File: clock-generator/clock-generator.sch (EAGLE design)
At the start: 39 parts, among them U1 SN74LVC1G04DBV, U3 ATSAMD11-QFN24, U4 SI5351C, X1 MINI-USB-SHIELD-UX60A-MB-5ST, X2 JACK2.5_SJ-2523

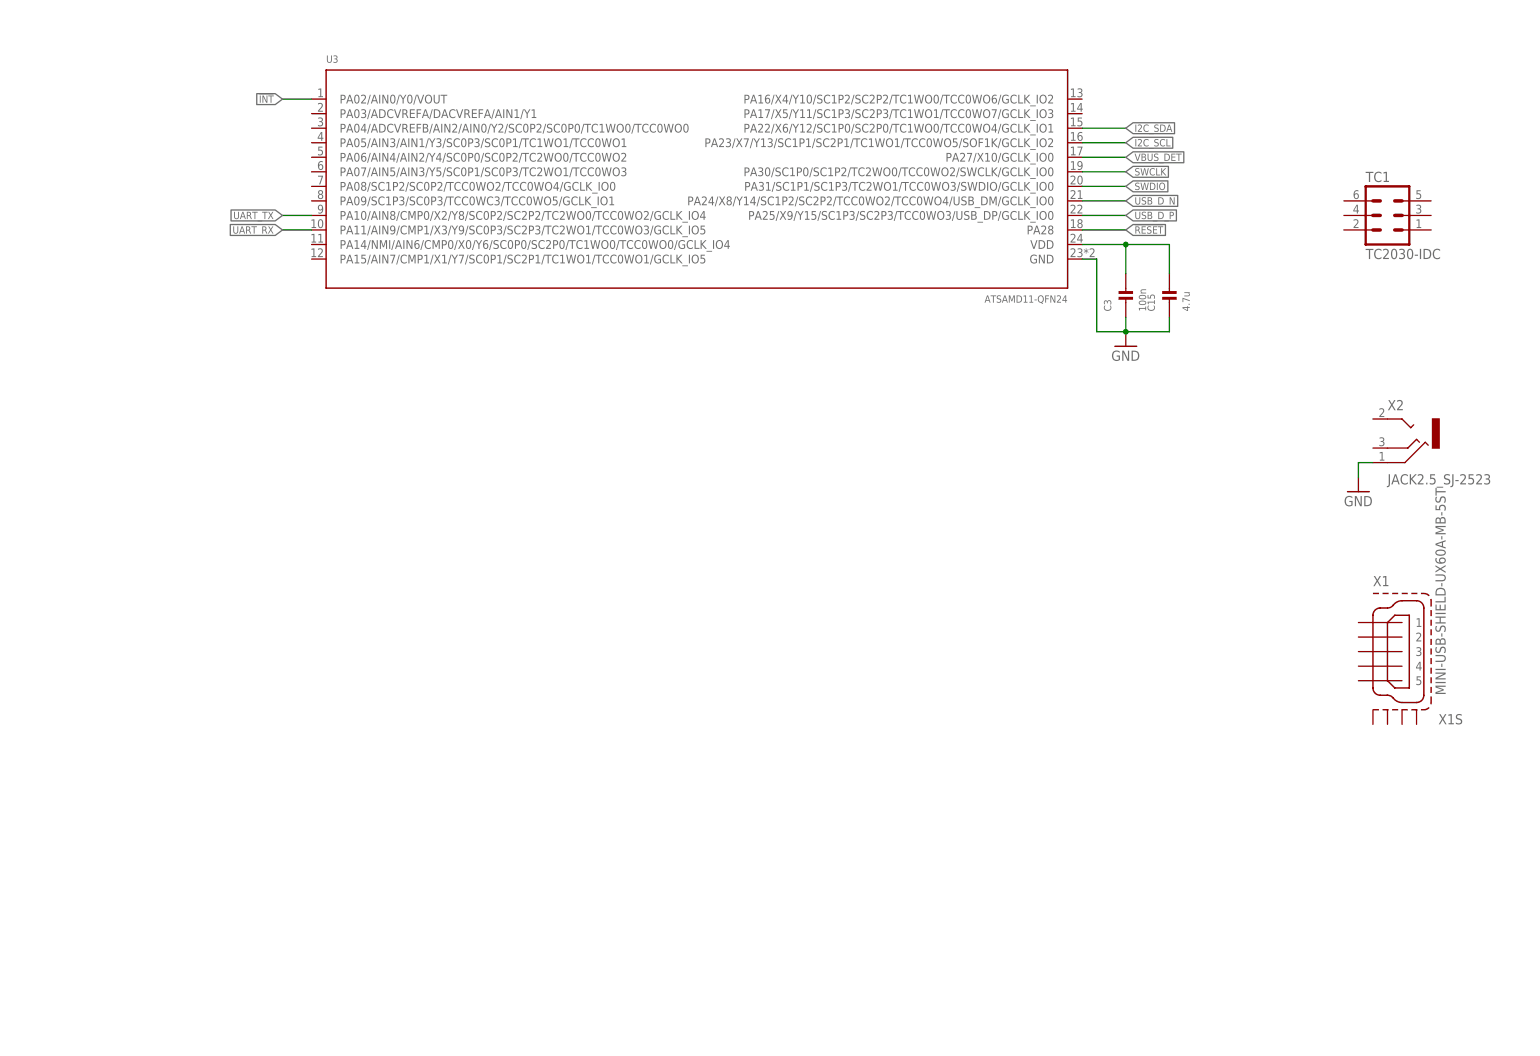
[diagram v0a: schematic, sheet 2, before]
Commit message: clock-generator: More work on schematics (USB, UART, ESD)
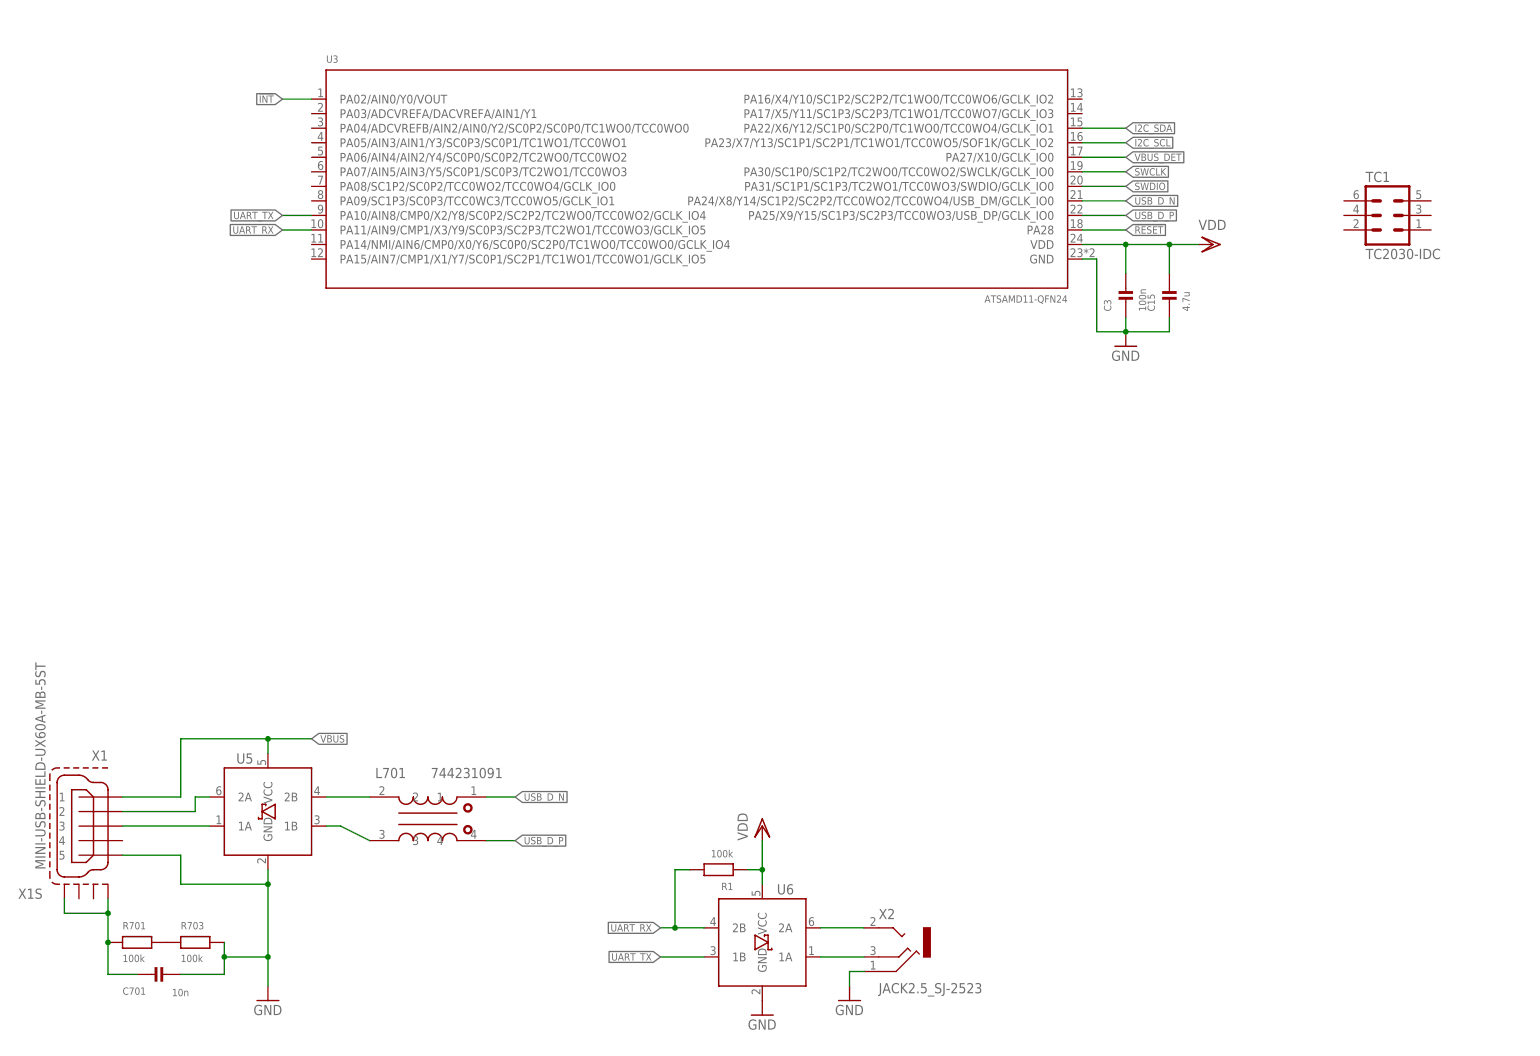
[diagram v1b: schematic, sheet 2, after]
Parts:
- added C701: 10n, rc-sysmocom:CAP_CERAMIC_0402
- added D1, D2, D3, D4, D5, D6, D7, D8, D9: 0603ESDA-TR, laforge:0603ESDA-TR
- added L701: 744231091, Wuerth_Elektronik_eiSos_V6_20140807:WE-CNSW_0805
- added R1, R701, R703: 100k, rc-sysmocom:RESISTOR_0603
- added R2, R3: 2k2, rc-sysmocom:RESISTOR_0603
- added U5, U6: IP4234CZ6, laforge:IP4234CZ6
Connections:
- removed net N$2: C15.2, C3.2, U3.VDD
- removed net N$4: JP1.1, R8.2, U1G1.I
- new net N$22: L701.2, U5.2B
- new net N$43: L701.3, U5.1B
- new net N$55: R701.1, R703.2
- new net N$6: U6.2A, X2.TIP
- new net N$61: C701.1, R701.2, X1S.S1, X1S.S4
- new net N$8: U6.1A, X2.MIDDLE
- new net USB0_D_N: U5.2A, X1G$1.2
- new net USB0_D_P: U5.1A, X1G$1.3
- new net VBUS: U5.VCC, X1G$1.1
- net CLK0_LINE: now also D1.K
- net CLK1_LINE: now also D2.K
- net CLK2_LINE: now also D3.K
- net CLK3_LINE: now also D4.K
- net CLK4_LINE: now also D5.K
- net CLK5_LINE: now also D6.K
- net CLK6_LINE: now also D7.K
- net CLK7_LINE: now also D8.K
- net CLKIN_AC: now also D9.K, JP1.1, R8.2, U1G1.I
- net GND: now also C701.2, D1.A, D2.A, D3.A, D4.A, D5.A, D6.A, D7.A, D8.A, D9.A, R703.1, U5.GND, U6.GND, X1G$1.5
- net I2C_SCL: now also R3.2
- net I2C_SDA: now also R2.2
- net UART_RX: now also R1.1, U6.2B
- net UART_TX: now also U6.1B
- net USB_D_N: now also L701.1
- net USB_D_P: now also L701.4
- net VDD: now also C15.2, C3.2, R1.2, R2.1, R3.1, U3.VDD, U6.VCC
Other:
- moved on the sheet: Q3, X1, X1S, X2

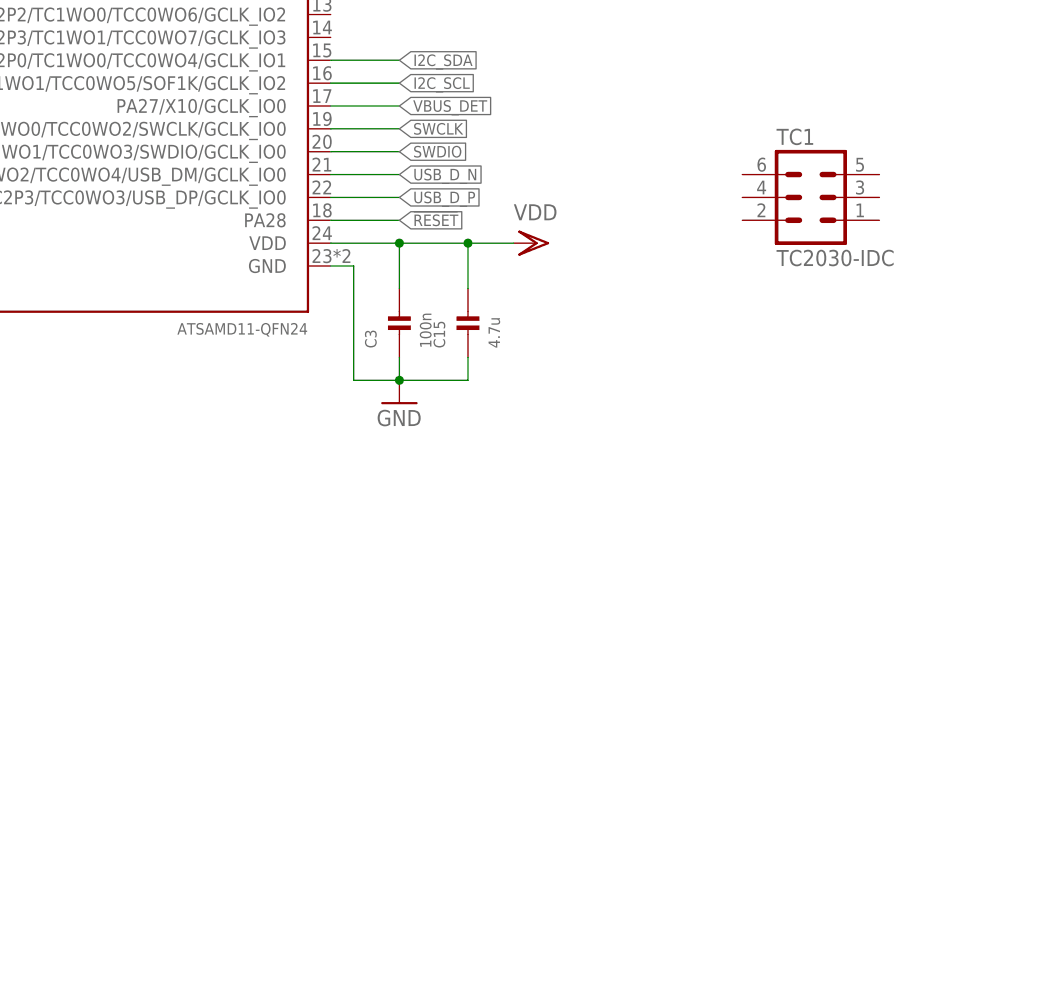
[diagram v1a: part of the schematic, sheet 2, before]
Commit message: clock-generator: More schematics work; initial placement/grouping
* add I2C EEPROM
* start board design file
* group parts to their respective "main part"
* define TC-2030 pinout
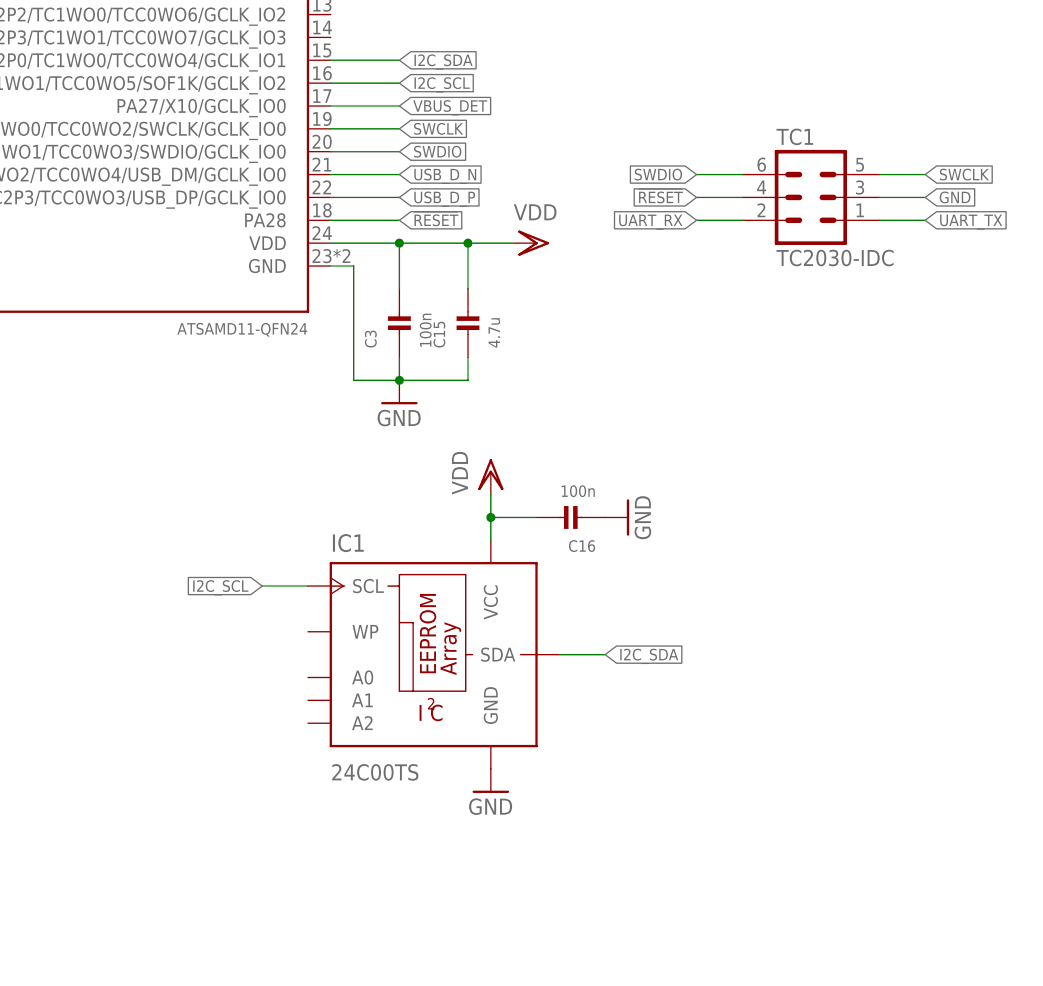
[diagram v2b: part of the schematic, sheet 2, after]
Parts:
- added C16: 100n, rc-sysmocom:CAP_CERAMIC_0402
- added IC1: 24C00TS, EEPROM-24C0x:24C00TS
- added X3: (no value), laforge:SMA-F-S-TH
- added X4: 1-227161-0, con-coax:1-227161-0
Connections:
- net !RESET: now also TC1.4
- net GND: now also C16.1, IC1.GND, TC1.3
- net I2C_SCL: now also IC1.SCL
- net I2C_SDA: now also IC1.SDA
- net SWCLK: now also TC1.5
- net SWDIO: now also TC1.6
- net UART_RX: now also TC1.2
- net UART_TX: now also TC1.1
- net VDD: now also C16.2, IC1.VCC
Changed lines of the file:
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@@
 <part name="D9" library="laforge" deviceset="0603ESDA-TR" device="" value=""/>
 <part name="GND35" library="SparkFun-Aesthetics" deviceset="GND" device=""/>
+<part name="IC1" library="EEPROM-24C0x" deviceset="24C0*" device="TS" technology="0"/>
+<part name="C16" library="rc-sysmocom" deviceset="CAP_CERAMIC" device="_0402" value="100n"/>
+<part name="GND36" library="supply1" deviceset="GND" device=""/>
+<part name="GND37" library="supply1" deviceset="GND" device=""/>
+<part name="VDD3" library="supply1" deviceset="VDD" device=""/>
+<part name="X3" library="laforge" deviceset="SMA-F" device="-S-TH"/>
+<part name="X4" library="con-coax" deviceset="?227161*" device="1-" technology="-0"/>
 </parts>
 <sheets>
@@
 <instance part="D9" gate="G$1" x="43.18" y="38.1"/>
 <instance part="GND35" gate="1" x="43.18" y="27.94"/>
+<instance part="X3" gate="G" x="127" y="142.24"/>
+<instance part="X4" gate="G$1" x="114.3" y="114.3"/>
 </instances>
 <busses>
@@
 <instance part="VDD1" gate="G$1" x="129.54" y="38.1"/>
 <instance part="VDD2" gate="G$1" x="208.28" y="139.7" rot="R270"/>
+<instance part="IC1" gate="G$1" x="195.58" y="96.52"/>
+<instance part="C16" gate="G$1" x="213.36" y="109.22" rot="R180"/>
+<instance part="GND36" gate="1" x="218.44" y="109.22" rot="R90"/>
+<instance part="GND37" gate="1" x="203.2" y="78.74"/>
+<instance part="VDD3" gate="G$1" x="203.2" y="114.3"/>
 </instances>
 <busses>
@@
 <pinref part="GND26" gate="1" pin="GND"/>
 </segment>
+<segment>
+<pinref part="TC1" gate="A" pin="3"/>
+<wire x1="246.38" y1="144.78" x2="251.46" y2="144.78" width="0.1524" layer="91"/>
+<label x="251.46" y="144.78" size="1.27" layer="95" xref="yes"/>
+</segment>
+<segment>
+<pinref part="C16" gate="G$1" pin="1"/>
+<pinref part="GND36" gate="1" pin="GND"/>
+</segment>
+<segment>
+<pinref part="IC1" gate="G$1" pin="GND"/>
+<pinref part="GND37" gate="1" pin="GND"/>
+</segment>
 </net>
 <net name="USB_D_N" class="0">
@@
 <label x="193.04" y="152.4" size="1.27" layer="95" xref="yes"/>
 </segment>
+<segment>
+<pinref part="TC1" gate="A" pin="5"/>
+<wire x1="246.38" y1="147.32" x2="251.46" y2="147.32" width="0.1524" layer="91"/>
+<label x="251.46" y="147.32" size="1.27" layer="95" xref="yes"/>
+</segment>
 </net>
 <net name="SWDIO" class="0">
@@
 <label x="193.04" y="149.86" size="1.27" layer="95" xref="yes"/>
 </segment>
+<segment>
+<pinref part="TC1" gate="A" pin="6"/>
+<wire x1="231.14" y1="147.32" x2="226.06" y2="147.32" width="0.1524" layer="91"/>
+<label x="226.06" y="147.32" size="1.27" layer="95" rot="R180" xref="yes"/>
+</segment>
 </net>
 <net name="UART_TX" class="0">
@@
 <wire x1="119.38" y1="15.24" x2="111.76" y2="15.24" width="0.1524" layer="91"/>
 <label x="111.76" y="15.24" size="1.27" layer="95" rot="R180" xref="yes"/>
+</segment>
+<segment>
+<pinref part="TC1" gate="A" pin="1"/>
+<wire x1="246.38" y1="142.24" x2="251.46" y2="142.24" width="0.1524" layer="91"/>
+<label x="251.46" y="142.24" size="1.27" layer="95" xref="yes"/>
 </segment>
 </net>
@@
 <junction x="114.3" y="20.32"/>
 </segment>
+<segment>
+<pinref part="TC1" gate="A" pin="2"/>
+<wire x1="231.14" y1="142.24" x2="226.06" y2="142.24" width="0.1524" layer="91"/>
+<label x="226.06" y="142.24" size="1.27" layer="95" rot="R180" xref="yes"/>
+</segment>
 </net>
 <net name="!RESET" class="0">
@@
 <label x="193.04" y="142.24" size="1.27" layer="95" xref="yes"/>
 </segment>
+<segment>
+<pinref part="TC1" gate="A" pin="4"/>
+<wire x1="231.14" y1="144.78" x2="226.06" y2="144.78" width="0.1524" layer="91"/>
+<label x="226.06" y="144.78" size="1.27" layer="95" rot="R180" xref="yes"/>
+</segment>
 </net>
 <net name="I2C_SDA" class="0">
@@
 <label x="193.04" y="160.02" size="1.27" layer="95" xref="yes"/>
 </segment>
+<segment>
+<pinref part="IC1" gate="G$1" pin="SDA"/>
+<wire x1="210.82" y1="93.98" x2="215.9" y2="93.98" width="0.1524" layer="91"/>
+<label x="215.9" y="93.98" size="1.27" layer="95" xref="yes"/>
+</segment>
 </net>
 <net name="I2C_SCL" class="0">
@@
 <wire x1="185.42" y1="157.48" x2="193.04" y2="157.48" width="0.1524" layer="91"/>
 <label x="193.04" y="157.48" size="1.27" layer="95" xref="yes"/>
+</segment>
+<segment>
+<pinref part="IC1" gate="G$1" pin="SCL"/>
+<wire x1="182.88" y1="101.6" x2="177.8" y2="101.6" width="0.1524" layer="91"/>
+<label x="177.8" y="101.6" size="1.27" layer="95" rot="R180" xref="yes"/>
 </segment>
 </net>
@@
 <junction x="200.66" y="139.7"/>
 </segment>
-</net>
+<segment>
+<pinref part="IC1" gate="G$1" pin="VCC"/>
+<wire x1="203.2" y1="106.68" x2="203.2" y2="109.22" width="0.1524" layer="91"/>
+<pinref part="C16" gate="G$1" pin="2"/>
+<wire x1="203.2" y1="109.22" x2="208.28" y2="109.22" width="0.1524" layer="91"/>
+<wire x1="203.2" y1="109.22" x2="203.2" y2="111.76" width="0.1524" layer="91"/>
+<junction x="203.2" y="109.22"/>
+<pinref part="VDD3" gate="G$1" pin="VDD"/>
+</segment>
+</net>
